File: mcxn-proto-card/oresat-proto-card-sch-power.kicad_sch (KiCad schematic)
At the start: 87 parts, among them Q1 DMP2240UDM, Q2 DMP3050LVT-7, Q7 DMP3050LVT-7, Q8 PMV45EN, Q9 PMV45EN, U10 TPS62111RSA, U11 MIC842LYC5, U12 MIC842LYC5, U2 MAX7310, U3 TS5A21366DCUR, U6 MAX4211FETE

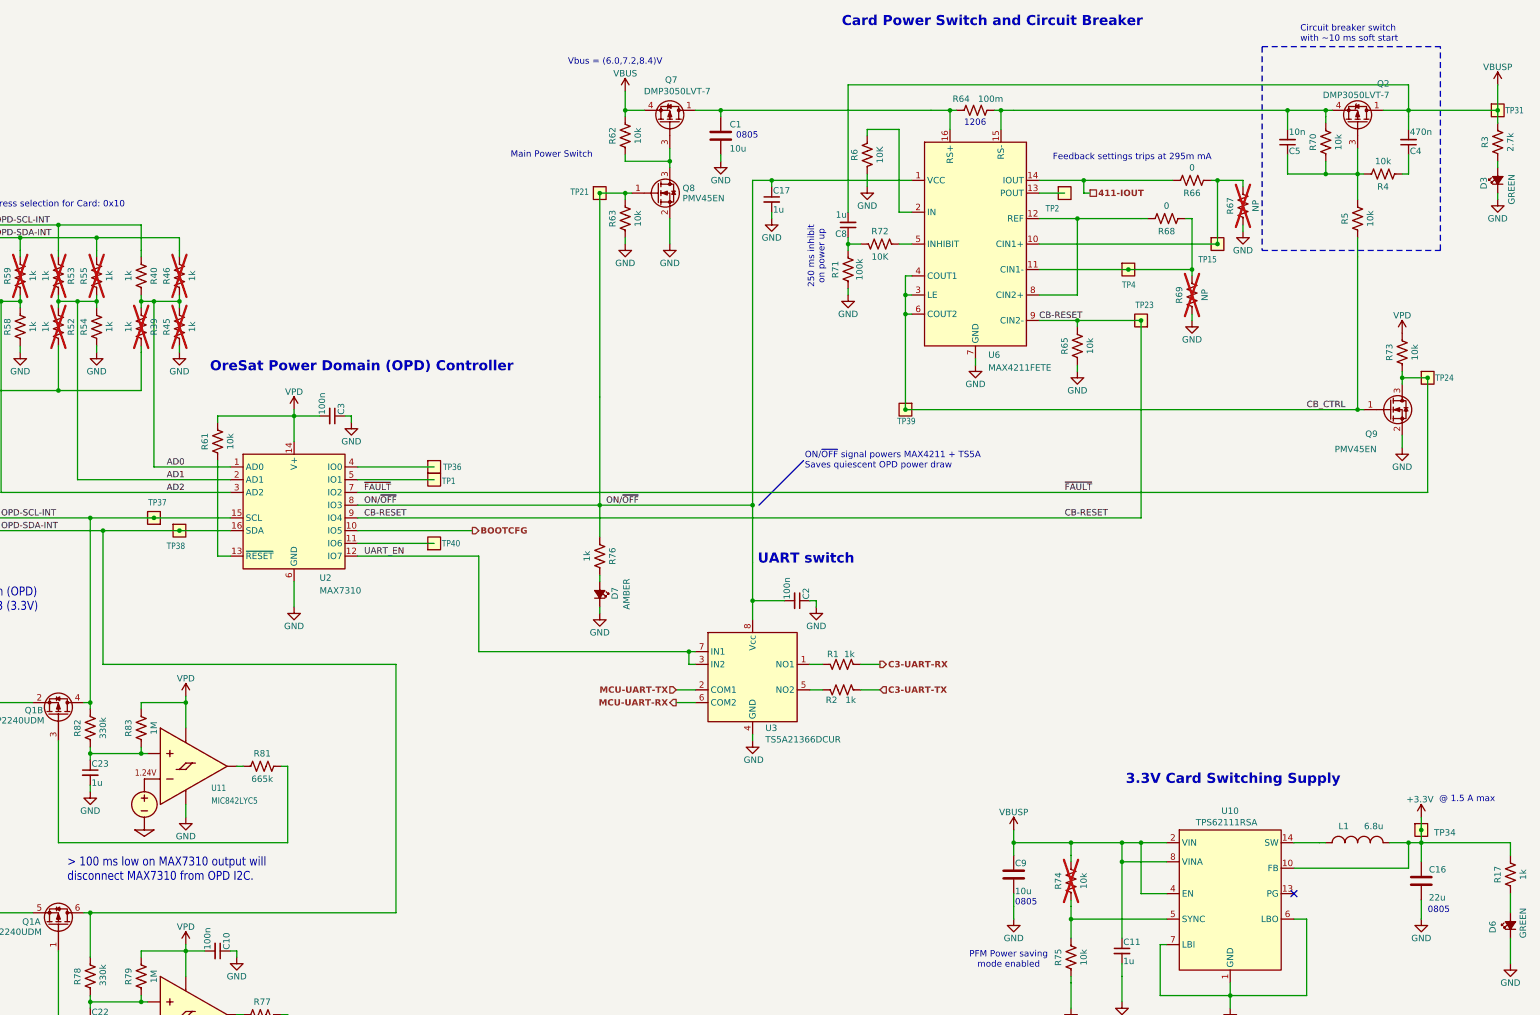
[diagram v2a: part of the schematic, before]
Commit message: BOM fixed; schematic polish (no change to PCB v6.0)
Fixed BOM, and synced with OreSat BOMs Google Sheet. Figured out large capacitor (> 4.7u) voltages and package issues, which are many. Set MCXN pin names to the right selection if possible.
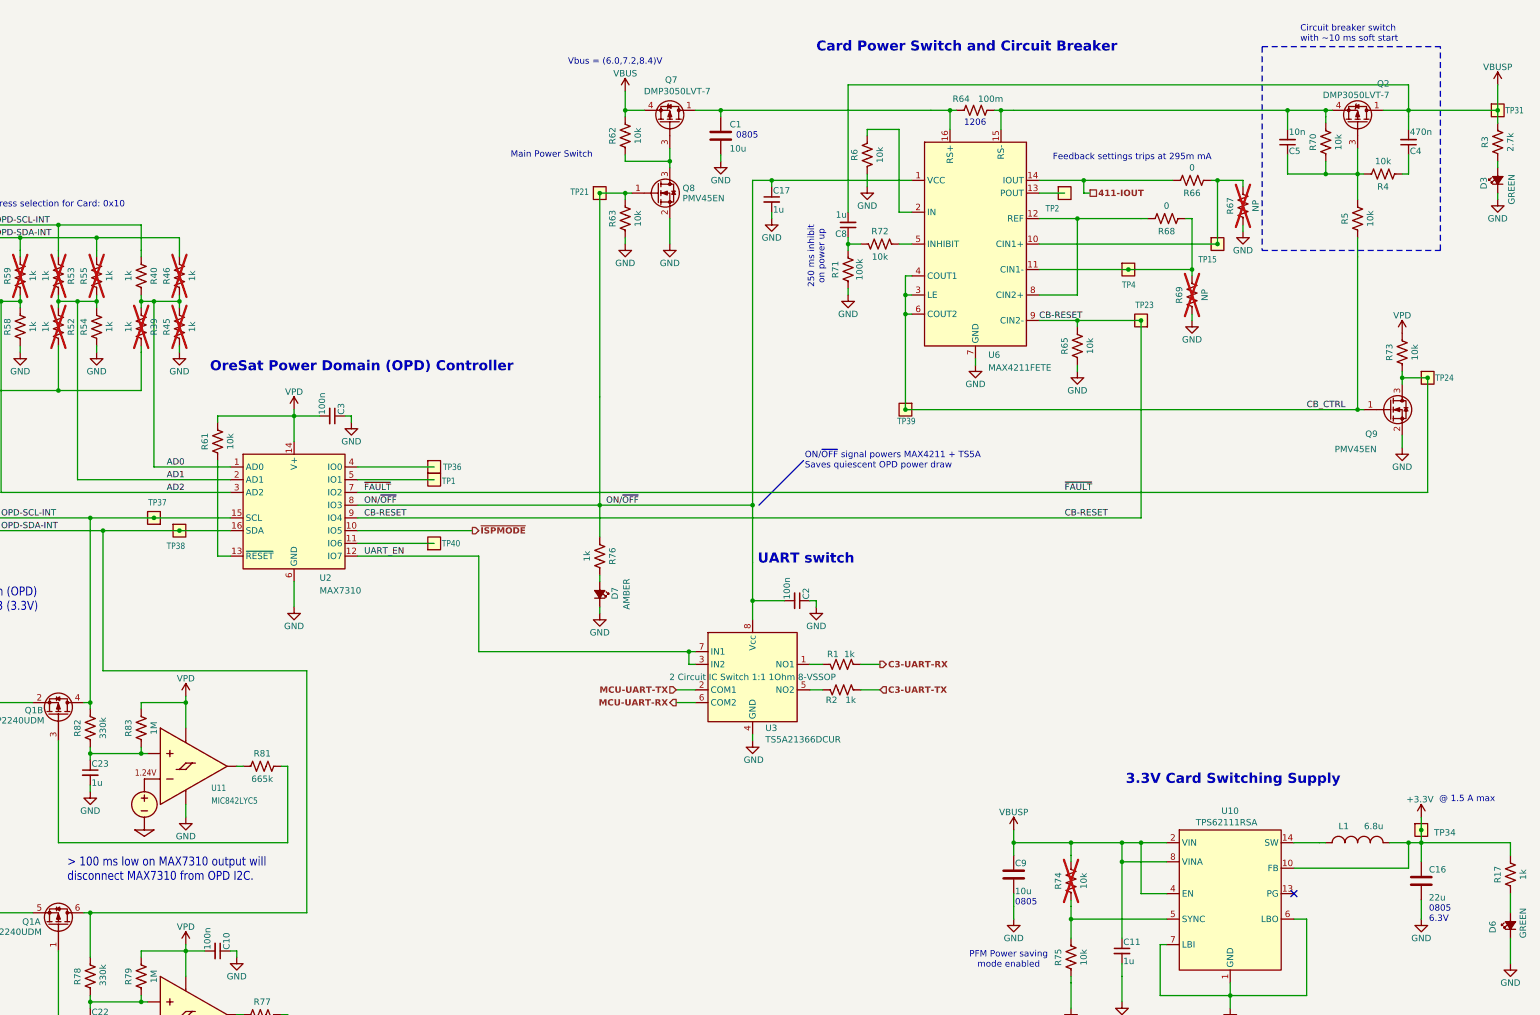
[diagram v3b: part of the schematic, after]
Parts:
- C1, C9: DIS Digi-Key -> DigiKey; DPN 1276-6472-1-ND -> 490-GRT21BC71E106KE13KCT-ND; MFR Samsung -> Murata Electronics; MPN CL21B106KOQNNNG -> GRT21BC71E106KE13K
- C10, C3: DIS Digi-Key -> DigiKey; DPN 399-14941-1-ND -> 399-6856-1-ND; MFR Kemet -> KEMET; MPN C0603C104K4PAC7867 -> C0603C104K5RACAUTO
- C11, C17, C22, C23: DIS Digi-Key -> DigiKey; DPN 311-1444-1-ND -> 490-GRT188R71E105KE13DCT-ND; MFR Yageo -> Murata Electronics; MPN CC0603KRX5R7BB105 -> GRT188R71E105KE13D
- C16: DIS Digi-Key -> DigiKey; DPN 490-9959-1-ND -> 478-KAM21AT70J226KUCT-ND; MFR Murata -> KYOCERA AVX; MPN GRM21BD71A226ME44L -> KAM21AT70J226KU
- C2: DIS (none) -> DigiKey; DPN (none) -> 399-6856-1-ND; MFR (none) -> KEMET; MPN (none) -> C0603C104K5RACAUTO
- C4: DIS (none) -> DigiKey; DPN (none) -> 399-C0603C474K3RACAUTOCT-ND; MFR (none) -> KEMET; MPN (none) -> C0603C474K3RACAUTO
- C5: DIS (none) -> DigiKey; DPN (none) -> 399-6851-1-ND; MFR (none) -> KEMET; MPN (none) -> C0603C103K5RACAUTO
- C8: DIS (none) -> DigiKey; DPN (none) -> 490-GRT188R71E105KE13DCT-ND; MFR (none) -> Murata Electronics; MPN (none) -> GRT188R71E105KE13D
- D3, D6: DIS Digi-Key -> DigiKey; DPN 511-1584-1-ND -> 732-4971-1-ND; MFR Rohm -> Wurth; MPN SML-E12M8WT86 -> 150060GS75000
- D7: DIS Digi-Key -> DigiKey; DPN 1830-1064-1-ND -> 732-150060AS75000CT-ND; MFR Inolux -> Wurth; MPN IN-S63AT5A -> 150060AS75000
- L1, Q1, Q2, Q7, Q8, Q9, U10, U2, U6: DIS Digi-Key -> DigiKey
- R1, R2: DIS (none) -> DigiKey; DPN (none) -> RMCF0603FT1K00CT-ND; MFR (none) -> Stackpole Electronics Inc; MPN (none) -> RMCF0603FT1K00
- R17, R76: DIS Digi-Key -> DigiKey; DPN (none) -> RMCF0603FT1K00CT-ND; MFR (none) -> Stackpole Electronics Inc; MPN (none) -> RMCF0603FT1K00
- R24: DIS Digi-Key -> DigiKey; DPN 311-10.0HRCT-ND -> RMCF0603FT10R0CT-ND; MFR Yageo -> Stackpole Electronics Inc; MPN RC0603FR-0710RL -> RMCF0603FT10R0
- R3: DIS Digi-Key -> DigiKey; DPN P2.7KDBCT-ND -> RMCF0603FT2K70CT-ND; MFR Panasonic -> Stackpole Electronics Inc; MPN ERA-3AEB272V -> RMCF0603FT2K70
- R4, R5: DIS (none) -> DigiKey; DPN (none) -> RMCF0603FT10K0CT-ND; MFR (none) -> Stackpole Electronics Inc; MPN (none) -> RMCF0603FT10K0
- R40, R54, R58: DIS Digi-Key -> DigiKey; DPN 1276-4275-1-ND -> RMCF0603FT1K00CT-ND; MFR Samsung -> Stackpole Electronics Inc; MPN RC1005F6653CS -> RMCF0603FT1K00
- R6, R72: value 10K -> 10k; DIS Digi-Key -> DigiKey; DPN 1276-4275-1-ND -> RMCF0603FT10K0CT-ND; MFR Samsung -> Stackpole Electronics Inc; MPN RC1005F6653CS -> RMCF0603FT10K0
- R60, R80: DIS Digi-Key -> DigiKey; DPN 311-100HRCT-ND -> RMCF0603FT100RCT-ND; MFR Yageo -> Stackpole Electronics Inc; MPN RC0603FR-07100RL -> RMCF0603FT100R
- R61, R62, R63, R65, R70, R73: DIS Digi-Key -> DigiKey; DPN RNCP0603FTD10K0CT-ND -> RMCF0603FT10K0CT-ND; MFR Stackpole -> Stackpole Electronics Inc; MPN RNCP0603FTD10K0 -> RMCF0603FT10K0
- R64: DIS Digi-Key -> DigiKey; DPN CSR1206FTR100CT-ND -> CSR1206FKR100CT-ND; MFR Stackpole -> Stackpole Electronics Inc; MPN CSR1206FTR100 -> CSR1206FKR100
- R66, R68: DIS Digi-Key -> DigiKey; DPN 311-0.0GRCT-ND -> RMCF0603ZT0R00CT-ND; MFR Yageo -> Stackpole Electronics Inc; MPN RC0603JR-070RL -> RMCF0603ZT0R00
- R71: DIS Digi-Key -> DigiKey; DPN 1276-4275-1-ND -> RMCF0603FT100KCT-ND; MFR Samsung -> Stackpole Electronics Inc; MPN RC1005F6653CS -> RMCF0603FT100K
- R75: DIS Digi-Key -> DigiKey; DPN 1276-4275-1-ND -> RMCF0603FT10K0CT-ND; MFR Samsung -> Stackpole Electronics Inc; MPN RC1005F6653CS -> RMCF0603FT10K0
- R77, R81: DIS Digi-Key -> DigiKey; DPN RNCP0603FTD10K0CT-ND -> RMCF0603FT665KCT-ND; MFR Stackpole -> Stackpole Electronics Inc; MPN RNCP0603FTD10K0 -> RMCF0603FT665K
- R78, R82: DIS Digi-Key -> DigiKey; DPN A129718CT-ND -> RMCF0603FT330KCT-ND; MFR TE Connectivity -> Stackpole Electronics Inc; MPN CRGCQ0603F330K -> RMCF0603FT330K
- R79, R83: DIS Digi-Key -> DigiKey; DPN 311-1.00MHRCT-ND -> RMCF0603FT1M00CT-ND; MFR Yageo -> Stackpole Electronics Inc; MPN RC0603FR-071ML -> RMCF0603FT1M00
- U11, U12: DIS (none) -> DigiKey; DPN (none) -> 576-2927-1-ND; MFR (none) -> Microchip; MPN (none) -> MIC842LYC5-TR
- U3: DIS (none) -> DigiKey; DPN (none) -> 296-24304-1-ND; MFR (none) -> Texas Instruments; MPN (none) -> TS5A21366DCUR
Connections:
- net BOOTCFG renamed ~{ISPMODE}
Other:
- note added: "0805 6.3V"
